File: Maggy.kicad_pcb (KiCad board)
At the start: 2 copper layers, 160 x 100 mm, 75 parts, among them CN1 0430450800, CN2 430451000, J1 XY308-2.54-2P, J2 XY308-2.54-2P, J3 XY308-2.54-2P, J4 XY308-2.54-2P, U1 CH224K, U10 INA214AIDCKR, U11 Socket for Teensy 4.1 (2x 1x2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, U12 INA214AIDCKR, U13 INA214AIDCKR, U14 TMAG5170A2DGKR, U15 TMAG5170A2DGKR, U16 TMAG5170A2DGKR, U17 TMAG5170A2DGKR, U18 TMAG5170A2DGKR, U2 A4950ELJTR-T, U3 A4950ELJTR-T, U4 A4950ELJTR-T, U5 A4950ELJTR-T, U6 TLV2372, U7 LM1117S-3.3, U8 LM1117S-5.0, U9 INA214AIDCKR

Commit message: chore: updated silkscreen text attributes
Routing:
- net (no net): track 244.0 -> 130.3 mm
- net UY_N_IN: track 33.4 -> 0.00 mm
- net UY_P_IN: track 27.4 -> 0.00 mm
- net UX_N_IN: track 23.1 -> 0.00 mm
- net UX_P_IN: track 23.0 -> 0.00 mm
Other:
- board text removed: "I2C"
- board text removed: "I2C-SCL2"
- board text removed: "I2C-SDA2"
- board text removed: "I2C_RST"
- board text removed: "I2C_SCL2"
- board text removed: "I2C_SDA2"

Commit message: chore: removed old sensor routing
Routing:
- net 3V3: track 485.9 -> 244.4 mm, vias 20 -> 12
- net GND: track 672.7 -> 434.2 mm, vias 29 -> 18
- net (no net): track 130.3 -> 93.0 mm, vias 4 -> 2
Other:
- board text removed: "Sensor0"
- board text removed: "Sensor1"
- board text removed: "Sensor2"
- board text removed: "Sensor3"
- board text removed: "Sensor4"
- board text removed: "Sensor5"
- board text removed: "Sensor6"
- board text removed: "Sensor7"

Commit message: fix: motor drivers mounted 180 degrees incorrect
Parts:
- turned U10 to 90 degrees
- turned U12 to 90 degrees
- turned U13 to 90 degrees
- turned U9 to 90 degrees
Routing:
- net +3V3: track 106.9 -> 0.00 mm, vias 2 -> 0
- net CUR_SOL1: track 0.00 -> 62.2 mm, vias 0 -> 1
- net CUR_SOL2: track 0.00 -> 44.7 mm, vias 0 -> 1

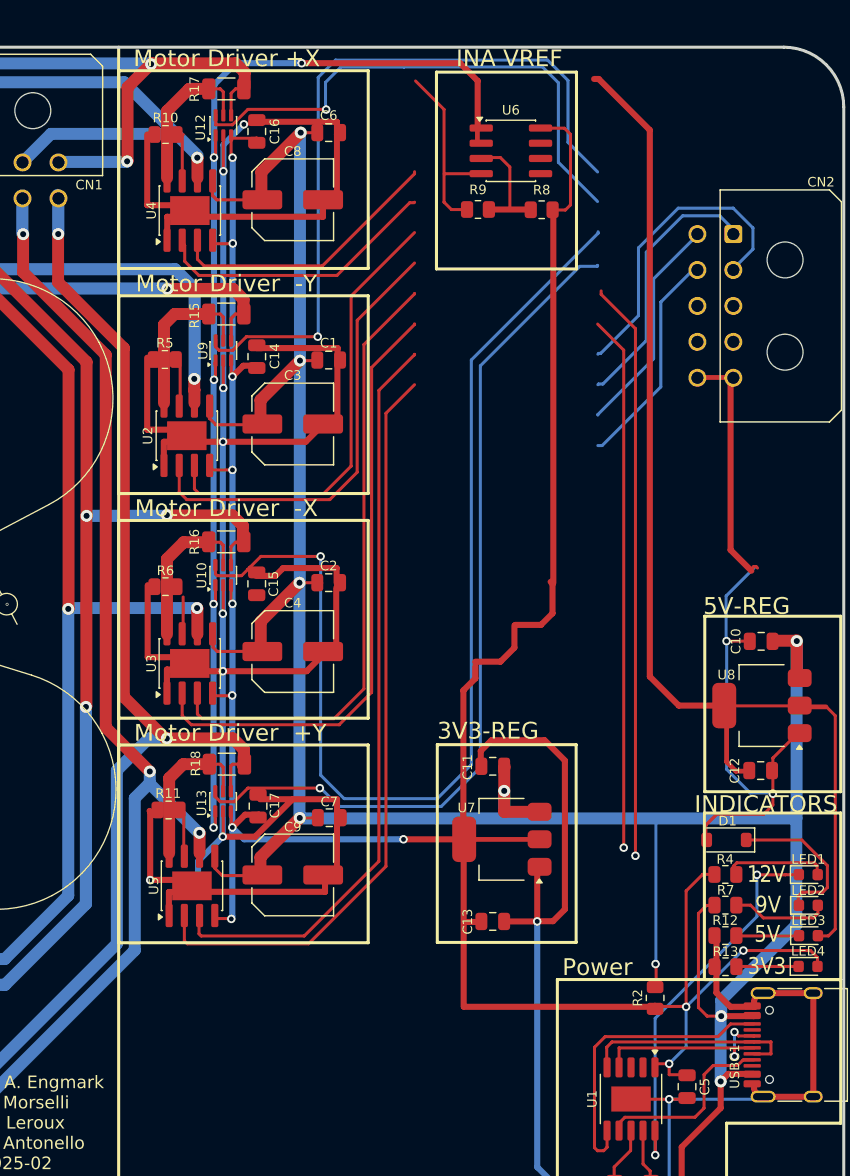
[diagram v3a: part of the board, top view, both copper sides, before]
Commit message: fix: flip capacitors to match schematic direction
Some capacitors were flipped the wrong way around compared to the schematic,
causing DRC errors complaining about shorts. Shouldn't really matter? Since
the capacitors are bi-directional.
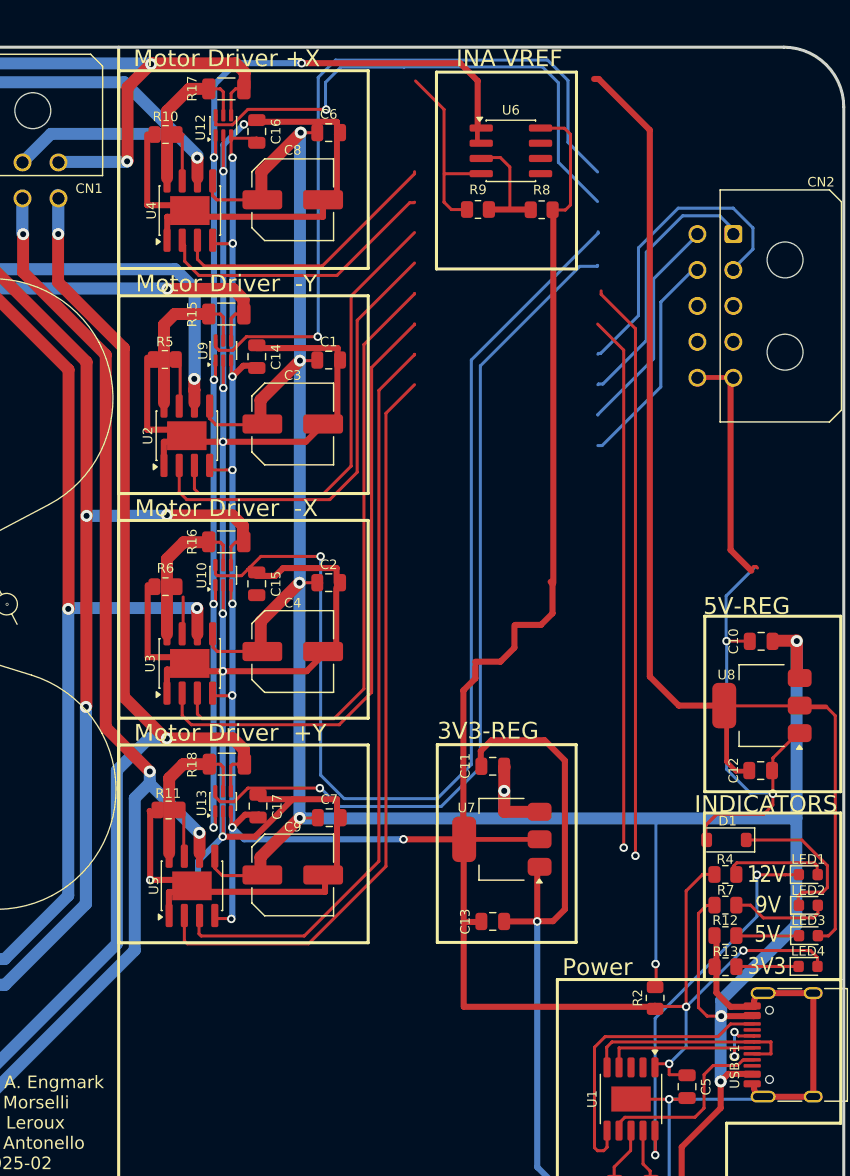
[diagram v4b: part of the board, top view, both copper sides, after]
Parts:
- turned C1 to 180 degrees
- turned C10 to 0 degrees
- turned C11 to 0 degrees
- turned C12 to 180 degrees
- turned C13 to 180 degrees
- turned C14 to 90 degrees
- turned C15 to 90 degrees
- turned C16 to 90 degrees
- turned C17 to 90 degrees
- turned C2 to 180 degrees
- turned C5 to 90 degrees
- turned C6 to 180 degrees
- turned C7 to 180 degrees
- turned R15 to 180 degrees
- turned R16 to 180 degrees
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
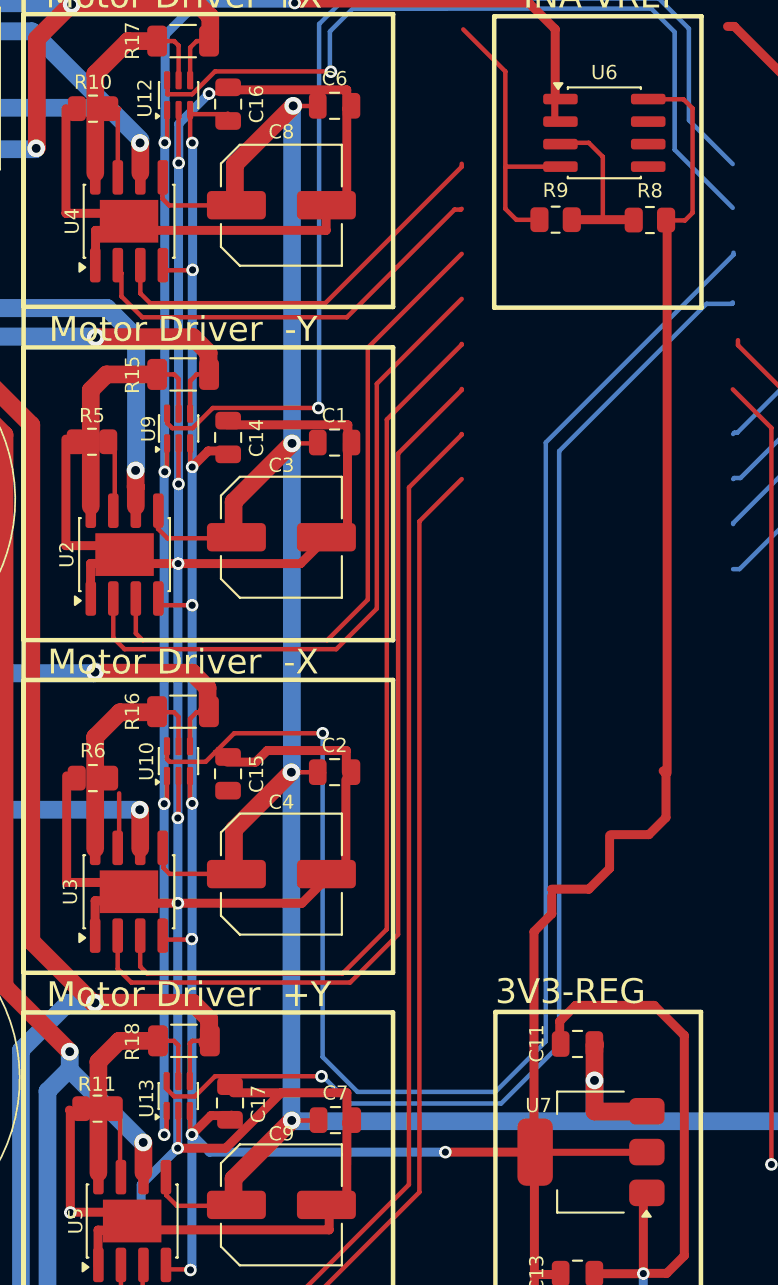
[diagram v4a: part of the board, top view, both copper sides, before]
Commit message: chore: remove incorrectly labelled nets, update tracks missing nets
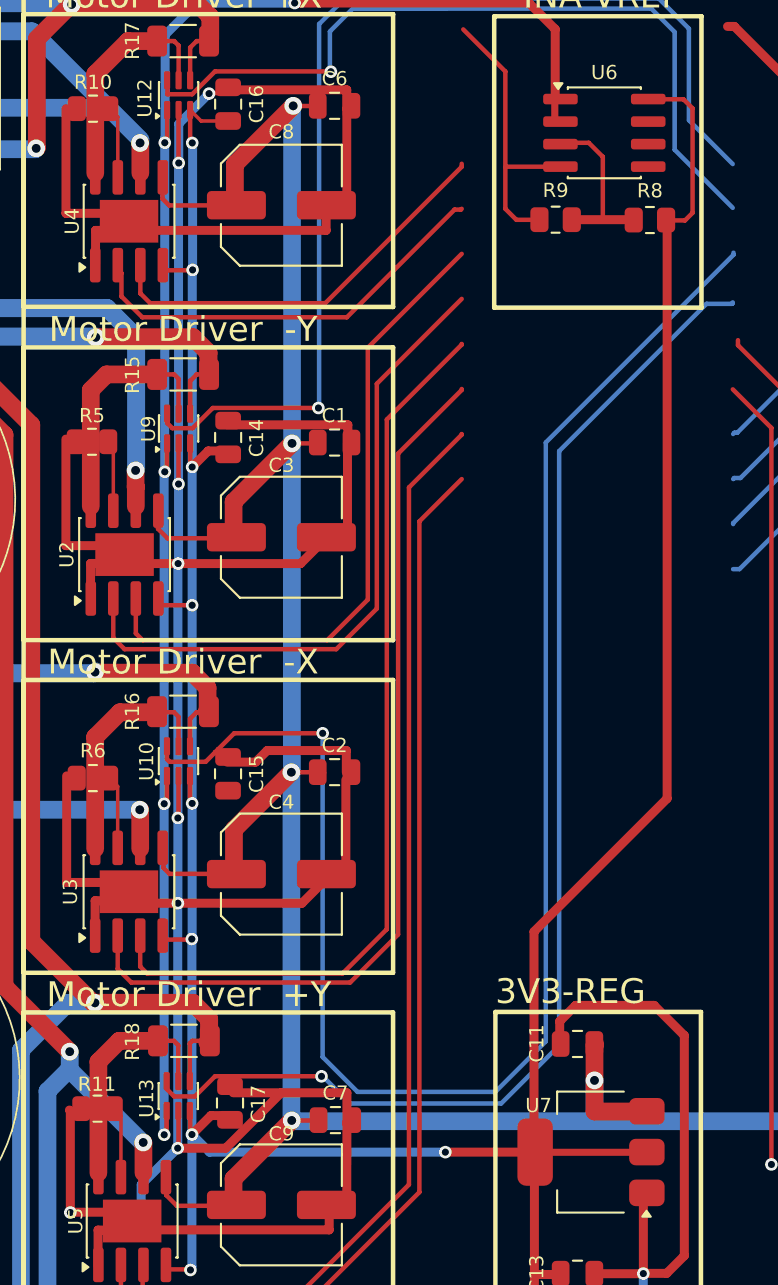
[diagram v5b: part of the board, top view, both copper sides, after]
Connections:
- net 1V65 renamed +1V65
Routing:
- net 3V3: track 244.4 -> 0.00 mm, vias 12 -> 0
- net +3V3: track 0.00 -> 242.4 mm, vias 0 -> 12
- net Net-(U4-LSS): track 0.00 -> 4.07 mm
- net Net-(U5-LSS): track 0.00 -> 4.03 mm
- net Net-(U2-LSS): track 0.00 -> 4.01 mm
- net $1N8651: track 3.66 -> 0.00 mm
- net $1N9221: track 3.46 -> 0.00 mm
- net $1N3748: track 3.16 -> 0.00 mm
- net Net-(U3-LSS): track 3.16 -> 4.13 mm

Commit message: chore: add teensy (socket) footprint to PCB
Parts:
- U11: footprint teensy:Teensy41 -> teensy:Teensy41_Socket_Only
- moved U11 78.3 mm to (201.8, 91.9), turned to -90 degrees
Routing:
- net (no net): track 93.0 -> 0.00 mm, vias 2 -> 0
- net unconnected-(U11-19_A5_SCL-Pad41): track 0.00 -> 48.3 mm, vias 0 -> 1
- net unconnected-(U11-18_A4_SDA-Pad40): track 0.00 -> 44.6 mm, vias 0 -> 1
- net CUR_SOL2: track 44.7 -> 66.4 mm
- net CUR_SOL1: track 62.2 -> 40.5 mm
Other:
- board text added: "SPI_CS_1"
- board text added: "SPI_CS_2"
- board text added: "SPI_CS_3"
- board text added: "SPI_CS_4"
- board text added: "SPI_CS_5"
- board text added: "SPI_MISO"
- board text added: "SPI_MOSI"
- board text added: "SPI_SCLK"
- board text added: "TMAG_ALERT"
- board text removed: "I2C_SCL"
- board text removed: "I2C_SDA"
